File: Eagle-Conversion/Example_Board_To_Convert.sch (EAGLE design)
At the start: 33 parts, among them J2 SMD, J3 PTH, J4 SMD, J6 SPI, U2 BNO080

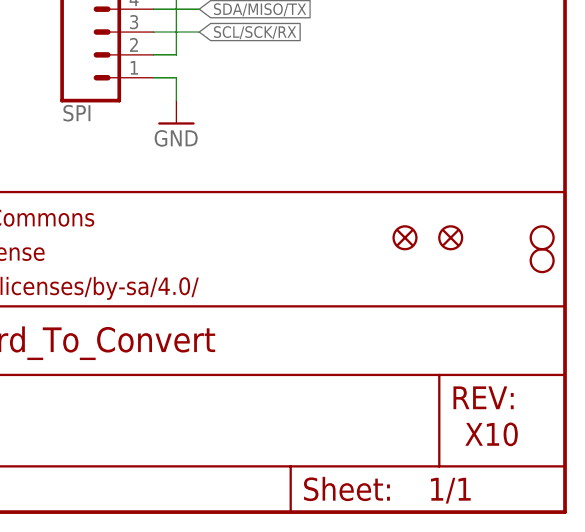
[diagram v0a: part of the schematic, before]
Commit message: Fixed some bugs and added possibility to turn of fiducial referencing and added a third mark to Nathans PCB example
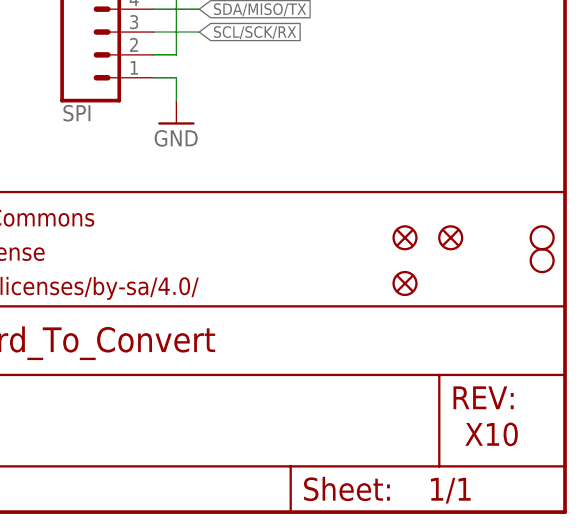
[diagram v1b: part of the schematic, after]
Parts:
- added JP1: FIDUCIALUFIDUCIAL, SparkFun:FIDUCIALUFIDUCIAL
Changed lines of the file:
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@@
 <part name="J5" library="SparkFun-Connectors" deviceset="CONN_01" device="PTH_NO_SILK_YES_STOP"/>
 <part name="J8" library="SparkFun-Connectors" deviceset="CONN_02" device="1X02_NO_SILK"/>
+<part name="JP1" library="SparkFun" deviceset="FIDUCIAL" device="UFIDUCIAL"/>
 </parts>
 <sheets>
@@
 <instance part="J5" gate="G$1" x="63.5" y="114.3"/>
 <instance part="J8" gate="G$1" x="20.32" y="30.48"/>
+<instance part="JP1" gate="G$1" x="231.14" y="25.4"/>
 </instances>
 <busses>
